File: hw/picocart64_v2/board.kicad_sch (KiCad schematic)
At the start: 68 parts

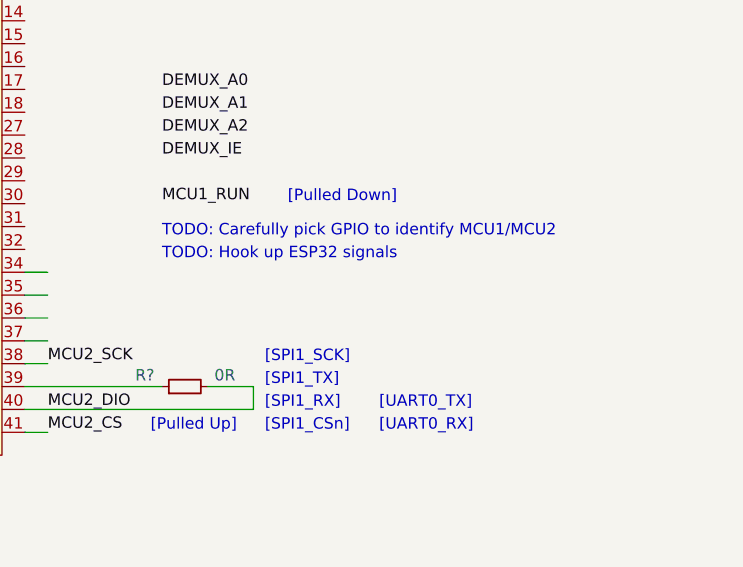
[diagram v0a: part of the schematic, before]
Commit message: Documented and figured out some stuff
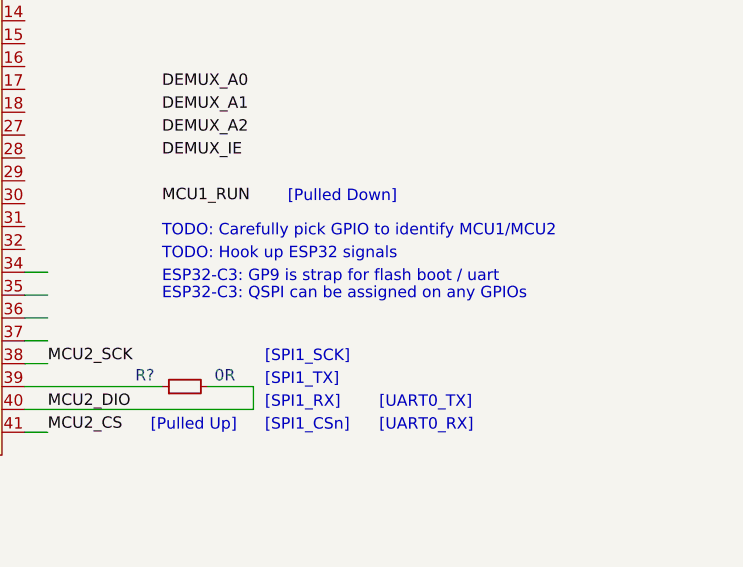
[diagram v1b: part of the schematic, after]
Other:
- note added: "ESP32-C3: GP9 is strap for flash boot / uart"
- note added: "ESP32-C3: QSPI can be assigned on any GPIOs"
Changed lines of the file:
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@@
+    (effects (font (size 1.27 1.27)) (justify left bottom))
+  )
+  (text "ESP32-C3: QSPI can be assigned on any GPIOs" (at 355.6 105.41 0)
     (effects (font (size 1.27 1.27)) (justify left bottom))
   )
@@
     (effects (font (size 1.27 1.27)) (justify left bottom))
   )
+  (text "ESP32-C3: GP9 is strap for flash boot / uart" (at 355.6 103.505 0)
+    (effects (font (size 1.27 1.27)) (justify left bottom))
+  )

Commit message: hw: v2 Finalize schematic
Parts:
- removed J?: Conn_01x10, symbol Connector_Generic:Conn_01x10
- removed R? (x2): 10K, symbol Device:R_Small
- added D1: WS2812B-2020, LED_SMD_Extra:WS2812B-2020, symbol LED_Extra:WS2812B-2020
- added J3: Conn_01x11, symbol Connector_Generic:Conn_01x11
- added JP1: SolderJumper_2_Open, symbol Jumper:SolderJumper_2_Open
- added R12: 10K, symbol Device:R_Small
- added R13, R18: 10k, symbol Device:R_Small
- added U16: ESP32-C3-WROOM-02, Espressif:ESP32-C3-WROOM-02, symbol Espressif:ESP32-C3-WROOM-02
- R16: renamed from R?; value 0R -> 470R
- gave numbers to parts that had none: 64
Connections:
- net +3V3: now also D1.4 (VDD), J3.11 (Pin_11), R12.2, R13.1, R18.1, U16.1 (3V3)
- net CIC_DCLK: now also U15.37 (GPIO25)
- net CIC_DIO: now also U15.36 (GPIO24)
- net DEMUX_A0: now also U15.18 (GPIO15)
- net DEMUX_A1: now also U15.27 (GPIO16)
- net DEMUX_A2: now also U15.28 (GPIO17)
- net DEMUX_IE: now also U15.29 (GPIO18)
- net GND: now also D1.2 (VSS), J3.10 (Pin_10), U16.19 (GND), U16.9 (GND)
- net MCU1_RUN: now also U15.30 (GPIO19), J3.9 (Pin_9)
- net MCU1_SWCLK: now also J3.8 (Pin_8)
- net MCU1_SWDIO: now also J3.7 (Pin_7)
- net MCU2_CS: now also J3.6 (Pin_6), R12.1
- net MCU2_SCK: now also R18.2
- net MCU2_SWCLK: now also J3.4 (Pin_4)
- net MCU2_SWDIO: now also J3.3 (Pin_3)
- net MCU2_UART_TX: now also U15.2 (GPIO0), J3.2 (Pin_2)
- net ~{COLD_RESET}: now also U15.34 (GPIO22)
- net ~{NMI}: now also U15.35 (GPIO23)
- net ESP32_D0_TX: now reaches U15.11 (GPIO8)
- net ESP32_D0_TX: now also U16.11 (GPIO20/U0RXD)
- net ESP32_D1_RX: now reaches U15.12 (GPIO9)
- net ESP32_D1_RX: now also U16.12 (GPIO21/U0TXD)
- net ESP32_D2_G9: now reaches U15.13 (GPIO10)
- net ESP32_D2_G9: now also U16.8 (GPIO9)
- net ESP32_D3: now reaches U15.14 (GPIO11)
- net ESP32_D3: now also U16.10 (GPIO10)
- net ESP32_CS: now reaches U15.15 (GPIO12)
- net ESP32_CS: now also U16.16 (GPIO2/ADC1_CH2)
- net ESP32_SCK: now reaches U15.16 (GPIO13)
- net ESP32_SCK: now also U16.7 (GPIO8)
- net ESP32_EN: now reaches U15.17 (GPIO14)
- net ESP32_EN: now also U16.2 (EN/CHIP_PU)
- net MCU2_RUN: now reaches U15.26 (RUN)
- net MCU2_RUN: now also J3.5 (Pin_5), R13.2
- net MCU2_UART_RX: now reaches U15.3 (GPIO1)
- net MCU2_UART_RX: now also J3.1 (Pin_1)
- net LED: now reaches U15.31 (GPIO20)
- net LED: now also D1.3 (DIN)
- net MCU2_GPIO21: now reaches U15.32 (GPIO21)
- net MCU2_GPIO21: now also JP1.1 (A)
- net at C12.2, U14.20 (XIN), Y1.3: now also JP1.2 (B)
- net SI_CLK: no longer names the net of U12.19 (SI_CLK)
- no-connect marks 15 -> 24
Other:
- note added: "BOM Optimization MCU2 CLK out replaces Xtal"
- note added: "ERC Note: SSI_SCLK is driven from multuple sources and it's OK."
- note added: "MCU1 <-> MCU2 communication 1. Backup solution, use SPI (PIO on MCU1, SPI slave on MCU2) 2. Backup solution, use UART MCU2_CS might function as MCU1_INT."
- note added: "MCU1/MCU2 boot sequence ------------------------ GPIO26 used to identify MCU1/MCU2 MCU1: Low (pulled down by DEMUX_IE) MCU2: High (pulled high by MCU2_SCK)"
- note added: "UART1_RX"
- note added: "UART1_TX"
- note added: "[MCU1_UART0_RX -> MCU2_TX]"
- note added: "[MCU1_UART0_TX -> MCU2_RX]"
- note added: "[PIO#1]"
- note added: "[PIO#2]"
- note added: "[clk_gpout0]"
- note removed: "ESP32-C3: GP9 is strap for flash boot / uart"
- note removed: "ESP32-C3: QSPI can be assigned on any GPIOs"
- note removed: "Hierarchial connections"
- note removed: "MCU1 <-> MCU2 communication 1. If possible, try SSI + MCU2_CS. Need to implement slave mode on MCU2 2. Backup solution, use SPI (PIO on MCU1, SPI slave on MCU2) 3. Backup solution, use SPI (PIO on MCU1, PIO on MCU2) 4. Backup solution, use UART MCU2_CS might function as MCU1_INT."
- note removed: "NOTE: MCU2_DIO and MCU2_CS are connected UART as well (backup solution)"
- note removed: "TODO: Add ESP32-C3-WROOM-02-H4"
- note removed: "TODO: Carefully pick GPIO to identify MCU1/MCU2"
- note removed: "TODO: Figure out if we want to use 0402 or 0603 resistor arrays"
- note removed: "TODO: Hook up ESP32 signals"
- note removed: "[UART0_RX -> MCU2_TX]"
- note removed: "[UART0_TX -> MCU2_RX]"
- moved on the sheet: C10, C11, C12, C13, C14, C15, C16, C17, C18, C19, C20, C21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

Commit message: hw: Routing progress
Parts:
- removed J3: Conn_01x11, symbol Connector_Generic:Conn_01x11
- added C38: 10u, Capacitor_SMD:C_0603_1608Metric, symbol Device:C_Small
- added C39: 100n, Capacitor_SMD:C_0402_1005Metric, symbol Device:C_Small
- added J3: Conn_02x06_Odd_Even, Connector_PinHeader_2.54mm:PinHeader_2x06_P2.54mm_Vertical_SMD, symbol Connector_Generic:Conn_02x06_Odd_Even
- added JP2, JP3: SolderJumper_2_Bridged, picocart64:SolderJumper-2_Small_Closed, symbol Jumper:SolderJumper_2_Bridged
- added R19: 10k, Resistor_SMD:R_0402_1005Metric, symbol Device:R_Small
- added R20: 100k, Resistor_SMD:R_0402_1005Metric, symbol Device:R_Small
- C10: value 10u7 -> 10u; footprint (none) -> Capacitor_SMD:C_0603_1608Metric
- C11: value 22u -> 10u; footprint (none) -> Capacitor_SMD:C_0603_1608Metric
- C12, C13, C14, C15, C16, C17, C18, C19, C20, C21, C22, C23, C24, C25, C26, C27, C28, C29, C30, C31, C32, C33, C34, C35, C36, C37: footprint (none) -> Capacitor_SMD:C_0402_1005Metric
- JP1: footprint (none) -> picocart64:SolderJumper-2_Small_Open
- R10, R11, R12, R13, R14, R15, R16, R17, R18, R4, R7, R8, R9: footprint (none) -> Resistor_SMD:R_0402_1005Metric
- R2, R3: value 1M -> 100k; footprint Resistor_SMD:R_0603_1608Metric -> Resistor_SMD:R_0402_1005Metric
- R5, R6: footprint Resistor_SMD:R_0603_1608Metric -> Resistor_SMD:R_0402_1005Metric
- RN1, RN2, RN3, RN4, RN5, RN6: footprint Resistor_SMD:R_Array_Convex_4x0603 -> Resistor_SMD:R_Array_Convex_4x0402
- TP1: value TP_MCU2_CS -> TP_MCU2_SCK; footprint (none) -> TestPoint:TestPoint_Pad_D1.0mm
- TP2: footprint (none) -> TestPoint:TestPoint_Pad_D1.0mm
- TP3: value MCU2_DIO -> TP_MCU2_DIO; footprint (none) -> TestPoint:TestPoint_Pad_D1.0mm
- U11: footprint (none) -> Package_TO_SOT_SMD:SOT-223
- Y1, Y2: footprint (none) -> Crystal:Crystal_SMD_2520-4Pin_2.5x2.0mm
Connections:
- net +3V3: now also C38.1, C39.1, J3.11 (Pin_11)
- net 3V3_USB: now also R20.2
- net AD0: now also RN4.1 (R1.1); no longer RN4.8 (R1.2)
- net AD0': now also RN4.8 (R1.2); no longer RN4.1 (R1.1)
- net AD1: now also RN4.2 (R2.1); no longer RN4.7 (R2.2)
- net AD1': now also RN4.7 (R2.2); no longer RN4.2 (R2.1)
- net AD2: now also RN4.3 (R3.1); no longer RN4.6 (R3.2)
- net AD2': now also RN4.6 (R3.2); no longer RN4.3 (R3.1)
- net AD3: now also RN4.4 (R4.1); no longer RN4.5 (R4.2)
- net AD3': now also RN4.5 (R4.2); no longer RN4.4 (R4.1)
- net AD4: now also RN5.3 (R3.1); no longer RN5.6 (R3.2)
- net AD4': now also RN5.6 (R3.2); no longer RN5.3 (R3.1)
- net AD5: now also RN5.4 (R4.1); no longer RN5.5 (R4.2)
- net AD5': now also RN5.5 (R4.2); no longer RN5.4 (R4.1)
- net AD6: now also RN6.2 (R2.1); no longer RN6.8 (R1.2)
- net AD6': now also RN6.7 (R2.2); no longer RN6.1 (R1.1)
- net AD7: now also RN6.1 (R1.1); no longer RN6.7 (R2.2)
- net AD7': now also RN6.8 (R1.2); no longer RN6.2 (R2.1)
- net ALEH: now also RN5.2 (R2.1); no longer RN5.7 (R2.2)
- net ALEH': now also RN5.7 (R2.2); no longer RN5.2 (R2.1)
- net ALEL: now also RN5.1 (R1.1); no longer RN5.8 (R1.2)
- net ALEL': now also RN5.8 (R1.2); no longer RN5.1 (R1.1)
- net CIC_DCLK: now also RN6.3 (R3.1); no longer RN6.6 (R3.2)
- net CIC_DCLK': now also RN6.6 (R3.2); no longer RN6.3 (R3.1)
- net ESP32_D0_TX: now also JP2.2 (B); no longer U16.11 (GPIO20/U0RXD)
- net ESP32_D1_RX: now also JP3.2 (B); no longer U16.12 (GPIO21/U0TXD)
- net ESP32_EN: now also R19.2
- net GND: now also C38.2, C39.2, J3.12 (Pin_12), R19.1, R20.1
- net MCU1_RUN: now also J3.10 (Pin_10)
- net MCU1_SWCLK: now also J3.8 (Pin_8)
- net MCU1_SWDIO: now also J3.6 (Pin_6)
- net MCU2_CS: now also J3.4 (Pin_4)
- net MCU2_GPIO21: now also J3.2 (Pin_2)
- net MCU2_RUN: now also J3.9 (Pin_9)
- net MCU2_SWCLK: now also J3.7 (Pin_7)
- net MCU2_SWDIO: now also J3.5 (Pin_5)
- net MCU2_UART_RX: now also J3.1 (Pin_1)
- net MCU2_UART_TX: now also J3.3 (Pin_3)
- net ~{INT1'}: now also RN6.5 (R4.2); no longer RN6.4 (R4.1)
- net ~{INT1}: now also RN6.4 (R4.1); no longer RN6.5 (R4.2)
- net MCU2_G27: now reaches R16.1, U15.39 (GPIO27)
- net MCU2_XOUT: now reaches C27.2, U15.21 (XOUT), Y2.1
- net MCU2_XIN: now reaches C26.2, U15.20 (XIN), Y2.3
- net MCU1_XOUT: now reaches C13.2, U14.21 (XOUT), Y1.1
- net MCU1_XIN: now reaches C12.2, JP1.2 (B), U14.20 (XIN), Y1.3
- new net: JP2.1 (A), U16.11 (GPIO20/U0RXD)
- new net: JP3.1 (A), U16.12 (GPIO21/U0TXD)
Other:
- note added: "Optional ESD protection PUSB3TB6"
- note added: "Pulled Down, powered down by default"
- note removed: "TODO: Do we need ESD protection?"
- moved on the sheet: C24, C25, RN4, RN5, RN6, U16
